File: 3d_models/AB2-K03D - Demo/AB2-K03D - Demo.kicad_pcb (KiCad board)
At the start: 2 copper layers, 182 parts

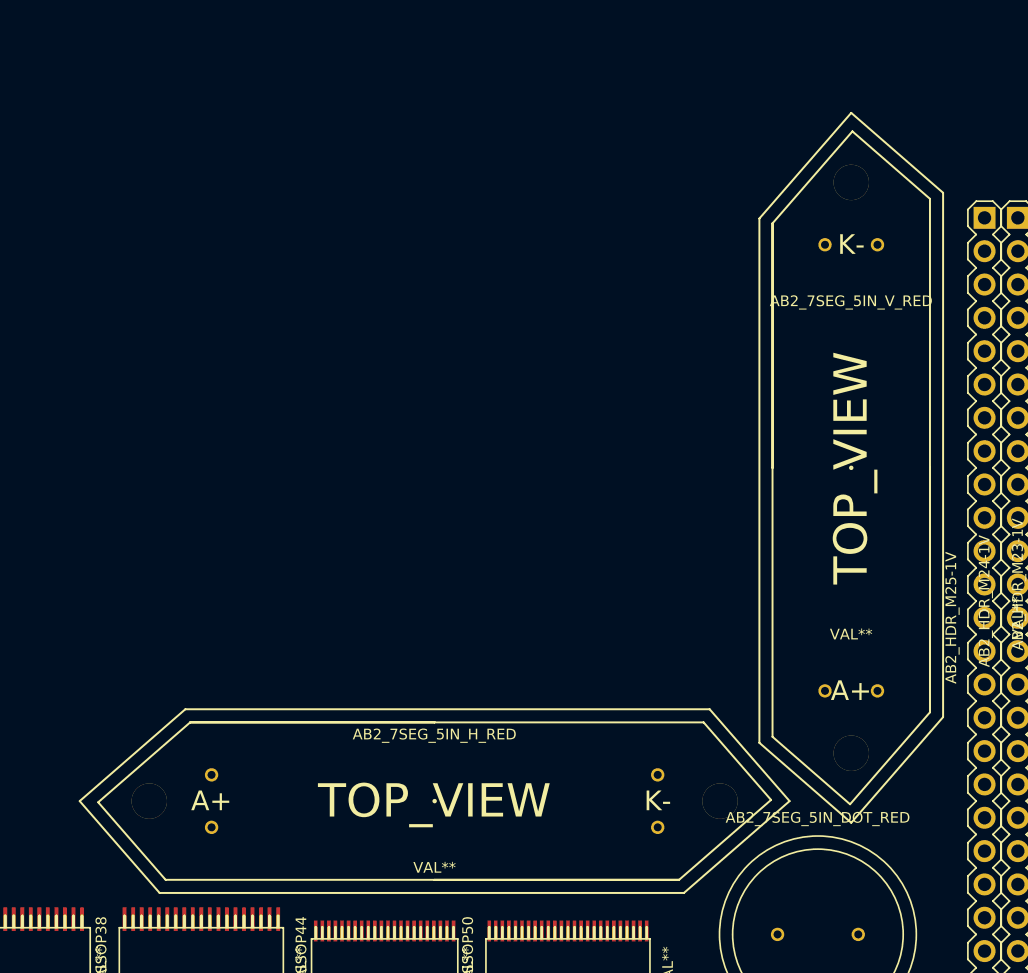
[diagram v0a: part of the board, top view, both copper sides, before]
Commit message: AB2-K03D: add 40mm heatsink/update micro usb
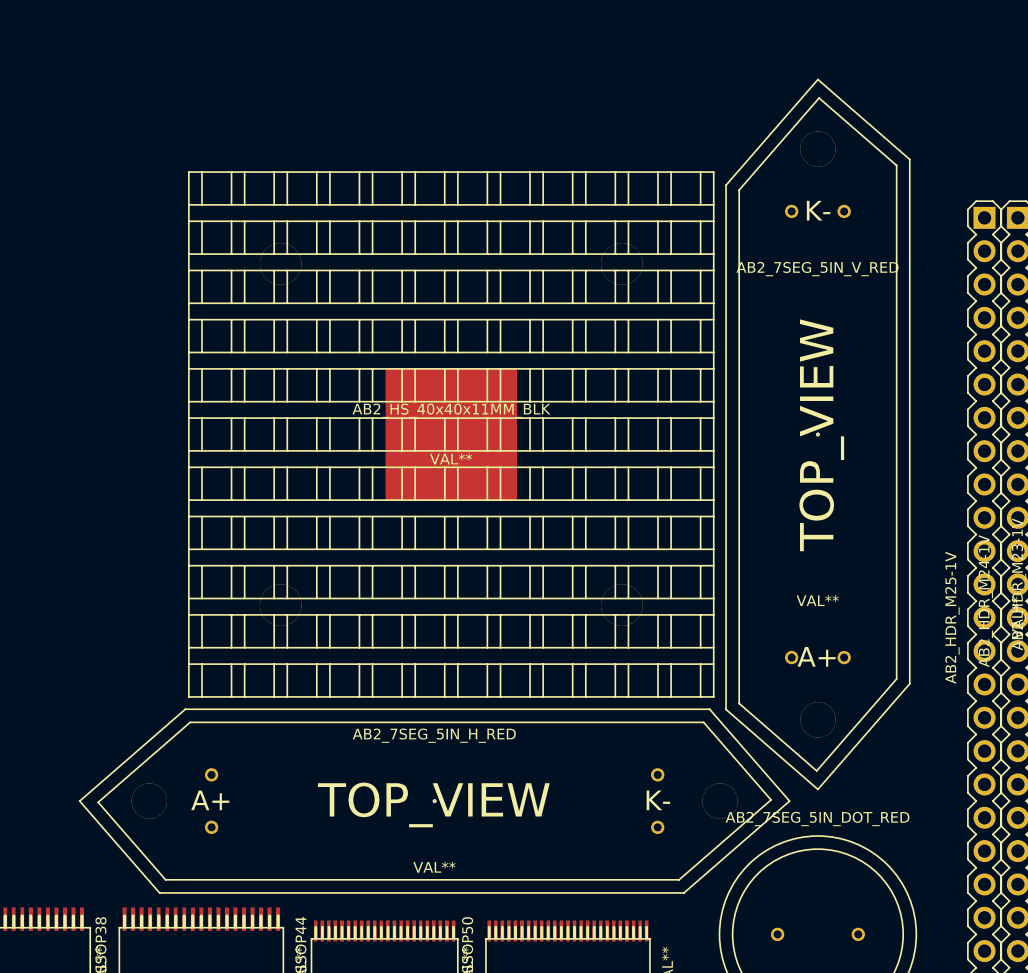
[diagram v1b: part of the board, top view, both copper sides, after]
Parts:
- added AB2_HS_40x40x11MM_BLK: VAL**, AB2_HS_40x40x11MM_BLK, F.Cu at (133.3, 201.9)
- moved AB2_7SEG_5IN_V_RED 3.59 mm to (161.3, 201.9)

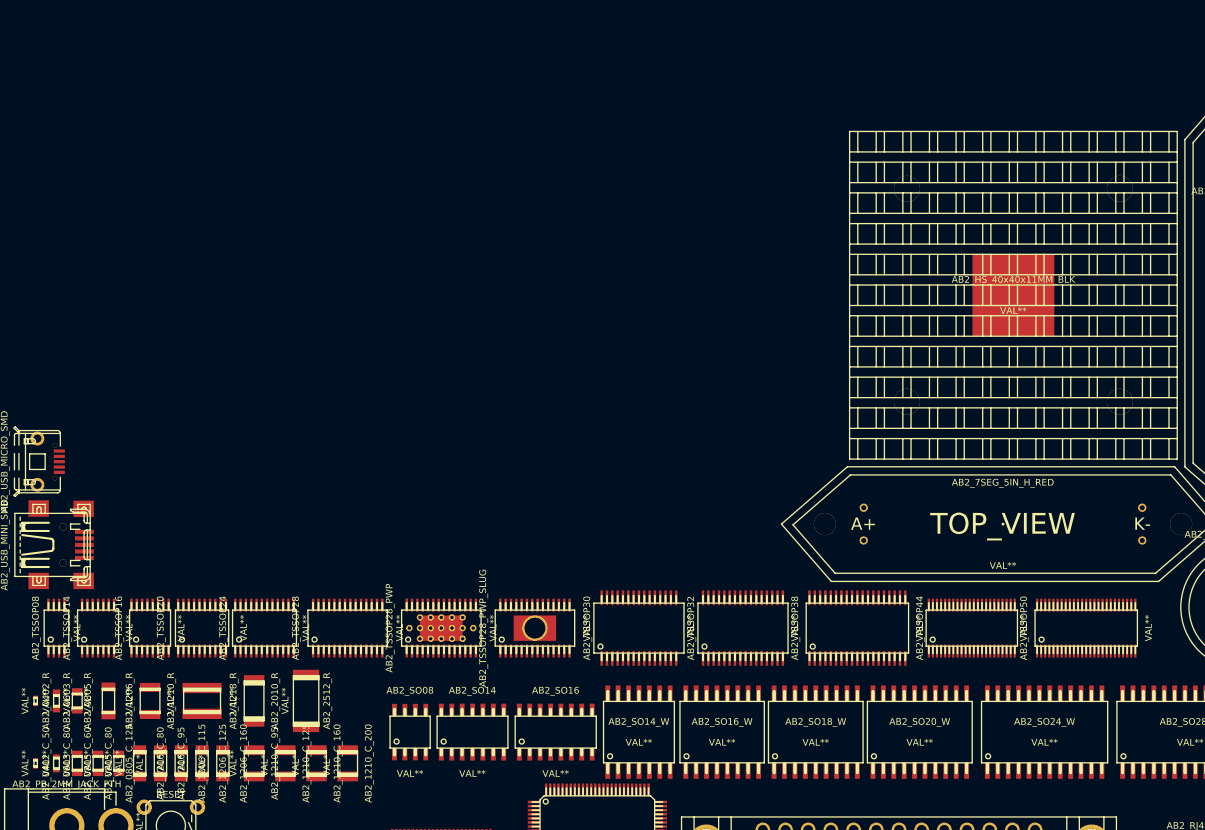
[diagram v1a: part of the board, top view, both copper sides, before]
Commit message: 3d: AB2-K03D: update silks soic/tssop update hsink
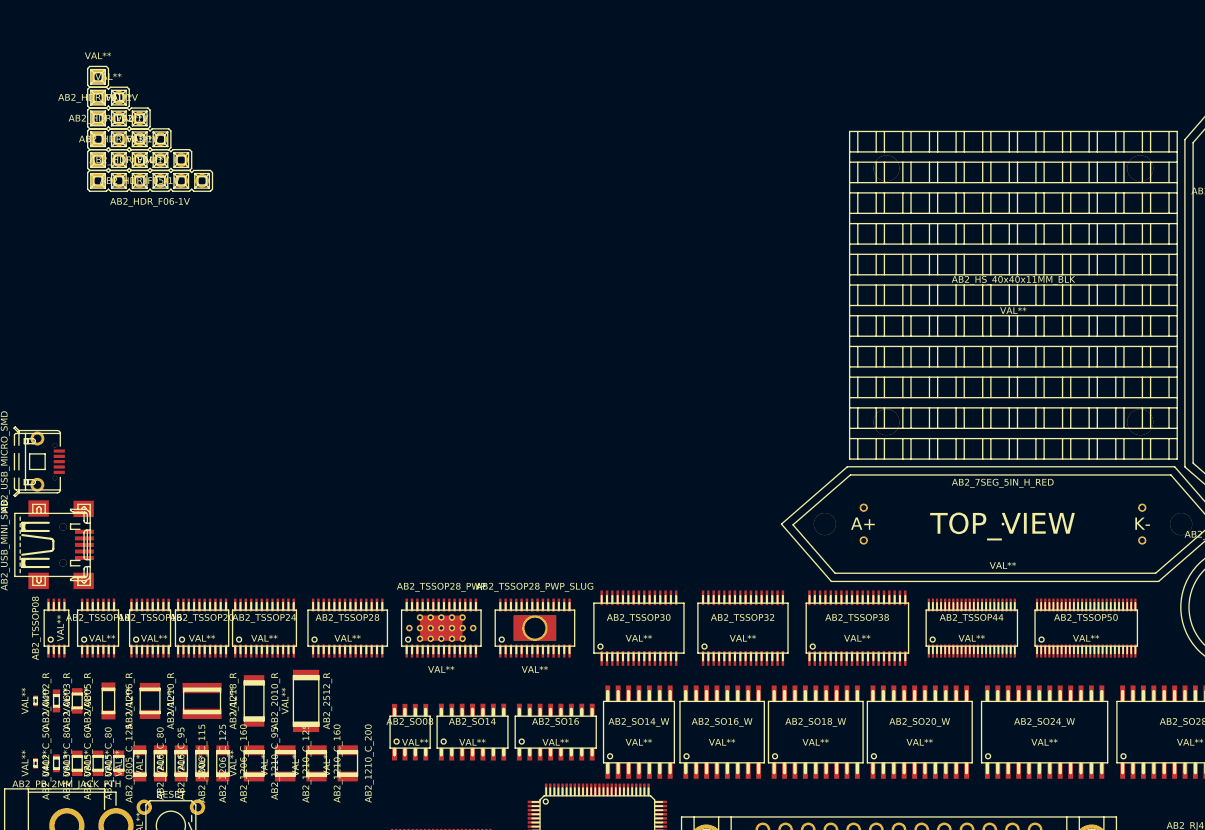
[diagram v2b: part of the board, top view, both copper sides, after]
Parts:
- added AB2_HDR_F01-1V: VAL**, AB2_HDR_F01-1V, F.Cu at (21.6, 175.3)
- added AB2_HDR_F02-1V: VAL**, AB2_HDR_F02-1V, F.Cu at (22.9, 177.8)
- added AB2_HDR_F03-1V: VAL**, AB2_HDR_F03-1V, F.Cu at (24.1, 180.3)
- added AB2_HDR_F04-1V: VAL**, AB2_HDR_F04-1V, F.Cu at (25.4, 182.9)
- added AB2_HDR_F05-1V: VAL**, AB2_HDR_F05-1V, F.Cu at (26.7, 185.4)
- added AB2_HDR_F06-1V: VAL**, AB2_HDR_F06-1V, F.Cu at (27.9, 188.0)

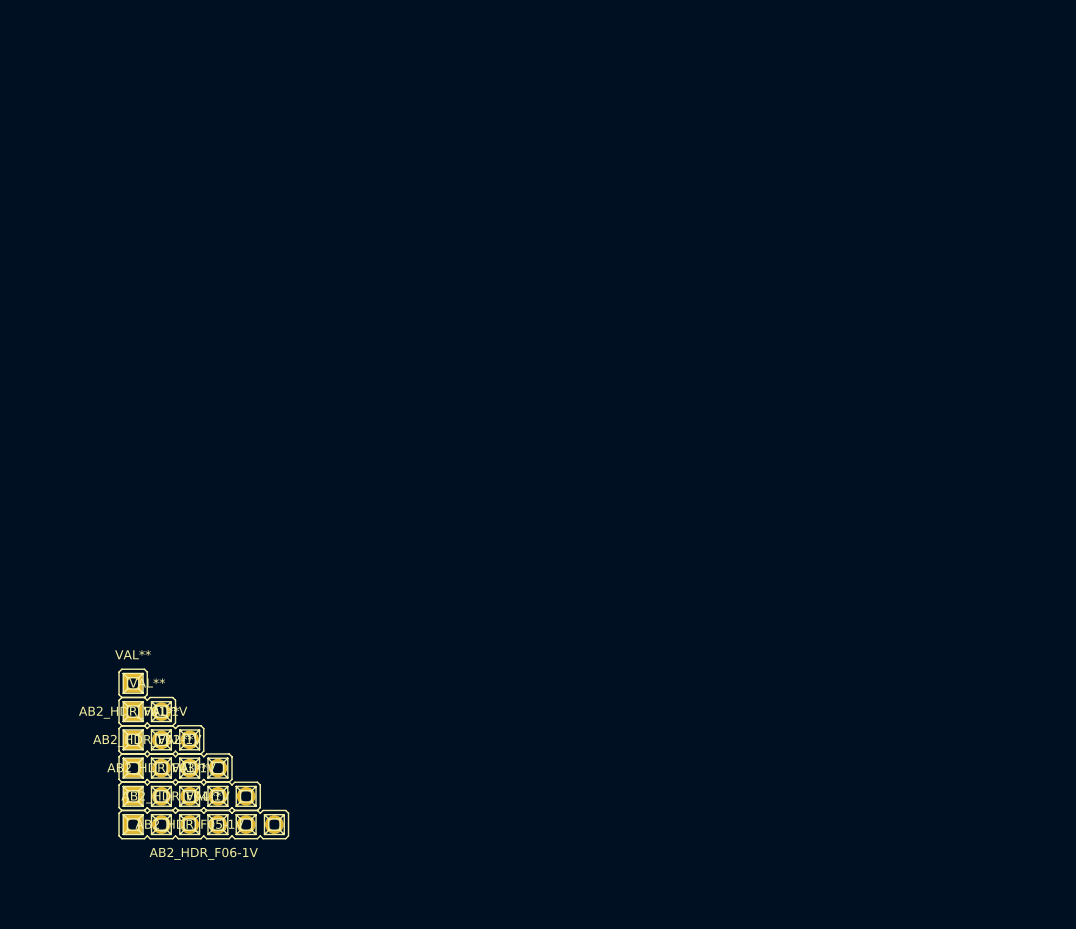
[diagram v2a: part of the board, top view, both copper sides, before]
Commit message: AB2-K03D: add all female vertical headers
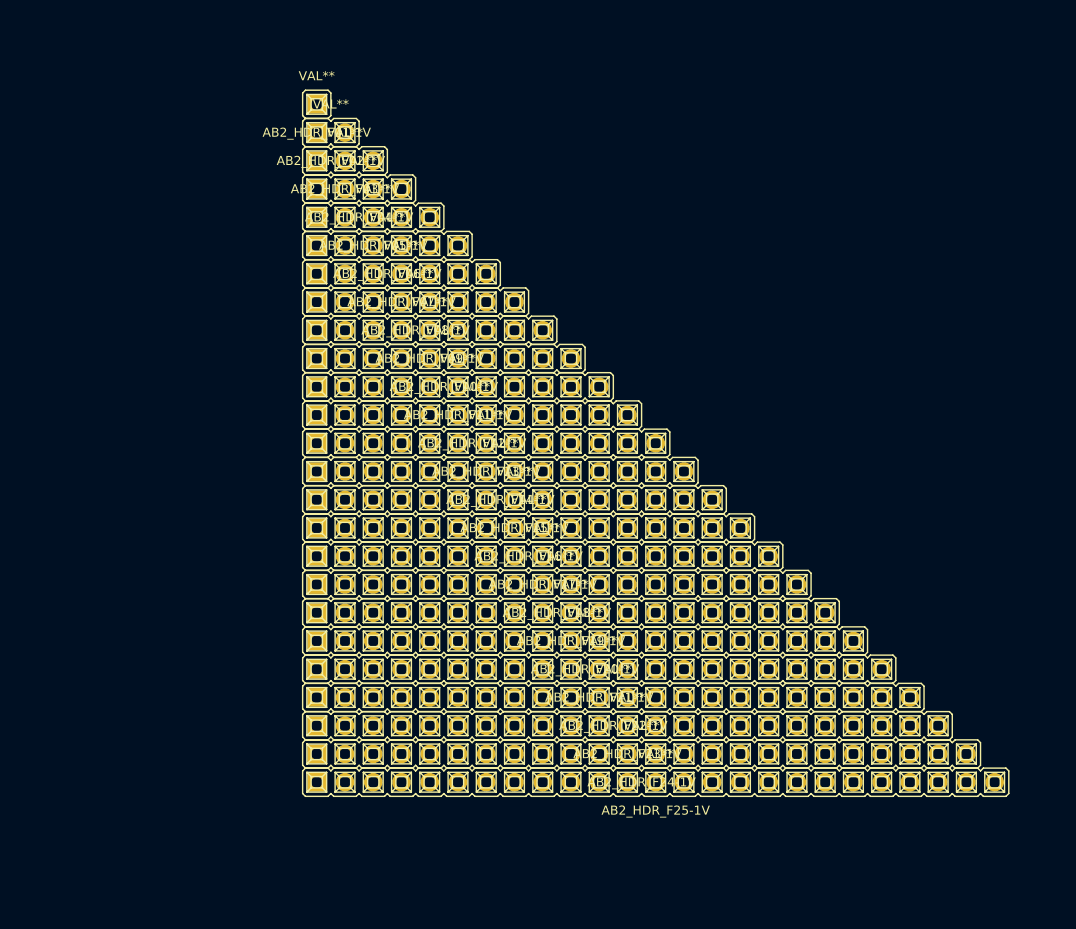
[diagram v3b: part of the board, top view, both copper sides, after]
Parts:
- added AB2_HDR_F07-1V: VAL**, AB2_HDR_F07-1V, F.Cu at (45.7, 138.4)
- added AB2_HDR_F08-1V: VAL**, AB2_HDR_F08-1V, F.Cu at (47.0, 141.0)
- added AB2_HDR_F09-1V: VAL**, AB2_HDR_F09-1V, F.Cu at (48.3, 143.5)
- added AB2_HDR_F10-1V: VAL**, AB2_HDR_F10-1V, F.Cu at (49.5, 146.1)
- added AB2_HDR_F11-1V: VAL**, AB2_HDR_F11-1V, F.Cu at (50.8, 148.6)
- added AB2_HDR_F12-1V: VAL**, AB2_HDR_F12-1V, F.Cu at (52.1, 151.1)
- added AB2_HDR_F13-1V: VAL**, AB2_HDR_F13-1V, F.Cu at (53.3, 153.7)
- added AB2_HDR_F14-1V: VAL**, AB2_HDR_F14-1V, F.Cu at (54.6, 156.2)
- added AB2_HDR_F15-1V: VAL**, AB2_HDR_F15-1V, F.Cu at (55.9, 158.8)
- added AB2_HDR_F16-1V: VAL**, AB2_HDR_F16-1V, F.Cu at (57.1, 161.3)
- added AB2_HDR_F17-1V: VAL**, AB2_HDR_F17-1V, F.Cu at (58.4, 163.8)
- added AB2_HDR_F18-1V: VAL**, AB2_HDR_F18-1V, F.Cu at (59.7, 166.4)
- added AB2_HDR_F19-1V: VAL**, AB2_HDR_F19-1V, F.Cu at (61.0, 168.9)
- added AB2_HDR_F20-1V: VAL**, AB2_HDR_F20-1V, F.Cu at (62.2, 171.4)
- added AB2_HDR_F21-1V: VAL**, AB2_HDR_F21-1V, F.Cu at (63.5, 174.0)
- added AB2_HDR_F22-1V: VAL**, AB2_HDR_F22-1V, F.Cu at (64.8, 176.5)
- added AB2_HDR_F23-1V: VAL**, AB2_HDR_F23-1V, F.Cu at (66.0, 179.1)
- added AB2_HDR_F24-1V: VAL**, AB2_HDR_F24-1V, F.Cu at (67.3, 181.6)
- added AB2_HDR_F25-1V: VAL**, AB2_HDR_F25-1V, F.Cu at (68.6, 184.2)
- moved AB2_HDR_F06-1V 54.6 mm to (44.5, 135.9)
- moved AB2_HDR_F02-1V 54.6 mm to (39.4, 125.7)
- moved AB2_HDR_F01-1V 54.6 mm to (38.1, 123.2)
- moved AB2_HDR_F03-1V 54.6 mm to (40.6, 128.3)
- moved AB2_HDR_F04-1V 54.6 mm to (41.9, 130.8)
- moved AB2_HDR_F05-1V 54.6 mm to (43.2, 133.3)
